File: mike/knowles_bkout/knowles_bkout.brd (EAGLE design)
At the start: 160 x 100 mm, 8 parts

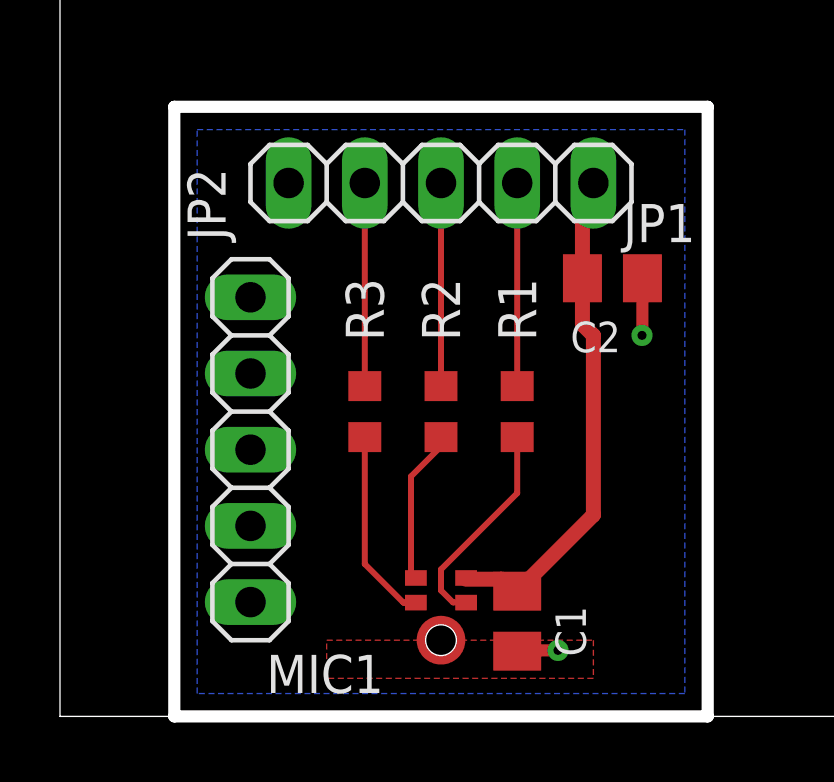
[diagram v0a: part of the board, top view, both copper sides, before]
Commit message: added leo footprint
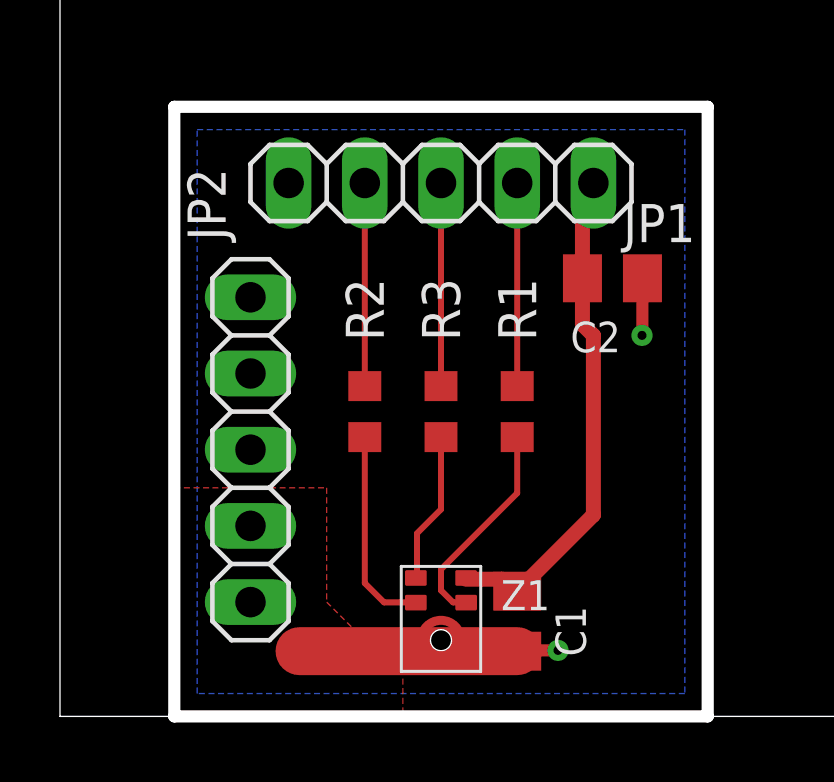
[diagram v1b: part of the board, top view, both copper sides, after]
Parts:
- removed MIC1: SPH0641LU4H-1, knowles_mic:SPH0641LU4H-1
- added Z1: SPH0641, SPH0641:SPH0641
- moved R2 2.54 mm to (10.2, 10.2)
- moved R3 2.54 mm to (12.7, 10.2)
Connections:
- net GND: now also Z1.3; no longer MIC1.3
- net N$2: now also R3.1; no longer R2.1
- net N$3: now also R2.1; no longer R3.1
- net N$5: now also Z1.1; no longer MIC1.2
- net N$6: now also Z1.2; no longer MIC1.1
- net N$7: now also Z1.4; no longer MIC1.4
- net VCC: now also Z1.5; no longer MIC1.5
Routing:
- net GND: track 3.28 -> 10.5 mm
- net N$6: track 5.18 -> 6.84 mm
- net N$5: track 6.47 -> 5.04 mm
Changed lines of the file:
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@@
 </autorouter>
 <elements>
-<element name="MIC1" library="knowles_mic" package="SPH0641LU4H-1" value="SPH0641LU4H-1" x="12.7" y="2.54" smashed="yes">
-<attribute name="NAME" x="6.88" y="0.78" size="1.27" layer="25"/>
-<attribute name="VALUE" x="8.18" y="6.84" size="1.27" layer="27"/>
-</element>
 <element name="C1" library="rcl" package="C0805K" value="100nF" x="15.24" y="3.175" smashed="yes" rot="R270">
 <attribute name="NAME" x="16.515" y="3.675" size="1.016" layer="25" rot="R270"/>
@@
 <attribute name="VALUE" x="13.335" y="10.795" size="1.27" layer="27" rot="R270"/>
 </element>
-<element name="R2" library="rcl" package="R0603" value="" x="12.7" y="10.16" smashed="yes" rot="R270">
+<element name="R2" library="rcl" package="R0603" value="" x="10.16" y="10.16" smashed="yes" rot="R270">
+<attribute name="NAME" x="9.525" y="14.605" size="1.27" layer="25" rot="R270"/>
+<attribute name="VALUE" x="8.255" y="10.795" size="1.27" layer="27" rot="R270"/>
+</element>
+<element name="R3" library="rcl" package="R0603" value="" x="12.7" y="10.16" smashed="yes" rot="R270">
 <attribute name="NAME" x="12.065" y="14.605" size="1.27" layer="25" rot="R270"/>
 <attribute name="VALUE" x="10.795" y="10.795" size="1.27" layer="27" rot="R270"/>
-</element>
-<element name="R3" library="rcl" package="R0603" value="" x="10.16" y="10.16" smashed="yes" rot="R270">
-<attribute name="NAME" x="9.525" y="14.605" size="1.27" layer="25" rot="R270"/>
-<attribute name="VALUE" x="8.255" y="10.795" size="1.27" layer="27" rot="R270"/>
 </element>
 <element name="JP2" library="pinhead" package="1X05" value="" x="6.35" y="8.89" smashed="yes" rot="R90">
@@
 <attribute name="VALUE" x="17.415" y="12.705" size="1.016" layer="27" display="off"/>
 </element>
+<element name="Z1" library="SPH0641" package="SPH0641" value="SPH0641" x="12.7" y="2.54"/>
 </elements>
 <signals>
 <signal name="GND">
 <contactref element="C1" pad="2"/>
-<contactref element="JP1" pad="1"/>
-<contactref element="JP2" pad="5"/>
-<contactref element="JP2" pad="4"/>
-<contactref element="JP2" pad="3"/>
-<contactref element="JP2" pad="2"/>
-<contactref element="JP2" pad="1"/>
 <contactref element="C2" pad="2"/>
 <polygon width="0.5" layer="16">
@@
 <wire x1="19.415" y1="12.715" x2="19.4" y2="12.7" width="0.4064" layer="1"/>
 <via x="19.4" y="12.7" extent="1-16" drill="0.3" diameter="0.6"/>
-<wire x1="15.24" y1="2.175" x2="15.265" y2="2.2" width="0.4064" layer="1"/>
 <wire x1="15.265" y1="2.2" x2="16.6" y2="2.2" width="0.4064" layer="1"/>
 <via x="16.6" y="2.2" extent="1-16" drill="0.3" diameter="0.6"/>
-<contactref element="MIC1" pad="3"/>
-<polygon width="0.2" layer="1" thermals="no">
-<vertex x="8.89" y="2.54"/>
-<vertex x="17.78" y="2.54"/>
-<vertex x="17.78" y="1.27"/>
-<vertex x="8.89" y="1.27"/>
+<contactref element="JP1" pad="1"/>
+<contactref element="JP2" pad="5"/>
+<contactref element="JP2" pad="4"/>
+<contactref element="JP2" pad="3"/>
+<contactref element="JP2" pad="2"/>
+<contactref element="JP2" pad="1"/>
+<contactref element="Z1" pad="3"/>
+<wire x1="15.24" y1="2.175" x2="7.985" y2="2.175" width="1.6" layer="1"/>
+<polygon width="0.45" layer="1">
+<vertex x="5.08" y="7.62"/>
+<vertex x="8.89" y="7.62"/>
+<vertex x="8.89" y="3.81"/>
+<vertex x="10.16" y="2.54"/>
+<vertex x="11.43" y="2.54"/>
+<vertex x="11.43" y="0"/>
+<vertex x="3.81" y="0"/>
+<vertex x="3.81" y="7.62"/>
 </polygon>
-<wire x1="15.24" y1="2.175" x2="12.7" y2="2.54" width="0" layer="19" extent="1-1"/>
+<wire x1="15.24" y1="2.175" x2="13.3625" y2="2.54" width="0" layer="19" extent="1-1"/>
 </signal>
 <signal name="VCC">
@@
 <wire x1="14.732" y1="4.175" x2="15.24" y2="4.175" width="0.5" layer="1"/>
 <wire x1="17.415" y1="17.415" x2="17.415" y2="14.605" width="0.5" layer="1"/>
-<contactref element="MIC1" pad="5"/>
 <contactref element="JP1" pad="5"/>
+<contactref element="Z1" pad="5"/>
 <wire x1="17.415" y1="17.415" x2="17.78" y2="17.78" width="0" layer="19" extent="1-1"/>
 <wire x1="13.5375" y1="4.614" x2="13.5375" y2="4.572" width="0" layer="19" extent="1-1"/>
@@
 <wire x1="15.24" y1="17.78" x2="15.24" y2="11.01" width="0.2" layer="1"/>
 </signal>
-<signal name="N$2">
-<contactref element="JP1" pad="3"/>
-<contactref element="R2" pad="1"/>
-<wire x1="12.7" y1="17.78" x2="12.7" y2="11.01" width="0.2" layer="1"/>
-</signal>
-<signal name="N$3">
-<contactref element="JP1" pad="2"/>
-<contactref element="R3" pad="1"/>
-<wire x1="10.16" y1="17.78" x2="10.16" y2="11.01" width="0.2" layer="1"/>
-</signal>
 <signal name="N$5">
-<contactref element="MIC1" pad="2"/>
 <contactref element="R3" pad="2"/>
-<wire x1="10.16" y1="9.31" x2="10.16" y2="5.08" width="0.2" layer="1"/>
-<wire x1="10.16" y1="5.08" x2="11.448" y2="3.792" width="0.2" layer="1"/>
-<wire x1="11.448" y1="3.792" x2="11.8625" y2="3.792" width="0.2" layer="1"/>
+<contactref element="Z1" pad="1"/>
+<wire x1="12.7" y1="9.31" x2="12.7" y2="6.9" width="0.2" layer="1"/>
+<wire x1="12.7" y1="6.9" x2="11.9" y2="6.1" width="0.2" layer="1"/>
+<wire x1="11.9" y1="6.1" x2="11.9" y2="4.6515" width="0.2" layer="1"/>
+<wire x1="11.9" y1="4.6515" x2="11.8625" y2="4.614" width="0.2" layer="1"/>
 </signal>
 <signal name="N$6">
-<contactref element="MIC1" pad="1"/>
 <contactref element="R2" pad="2"/>
-<wire x1="11.8625" y1="4.614" x2="11.7" y2="4.7765" width="0.2" layer="1"/>
-<wire x1="11.7" y1="4.7765" x2="11.7" y2="8" width="0.2" layer="1"/>
-<wire x1="11.7" y1="8" x2="12.7" y2="9" width="0.2" layer="1"/>
-<wire x1="12.7" y1="9" x2="12.7" y2="9.31" width="0.2" layer="1"/>
+<contactref element="Z1" pad="2"/>
+<wire x1="10.16" y1="9.31" x2="10.16" y2="4.44" width="0.2" layer="1"/>
+<wire x1="10.16" y1="4.44" x2="10.8" y2="3.8" width="0.2" layer="1"/>
+<wire x1="10.8" y1="3.8" x2="11.8545" y2="3.8" width="0.2" layer="1"/>
+<wire x1="11.8545" y1="3.8" x2="11.8625" y2="3.792" width="0.2" layer="1"/>
 </signal>
 <signal name="N$7">
-<contactref element="MIC1" pad="4"/>
 <contactref element="R1" pad="2"/>
-<wire x1="13.5375" y1="3.792" x2="13.5295" y2="3.8" width="0.2" layer="1"/>
 <wire x1="13.5295" y1="3.8" x2="13.1" y2="3.8" width="0.2" layer="1"/>
 <wire x1="13.1" y1="3.8" x2="12.7" y2="4.2" width="0.2" layer="1"/>
@@
 <wire x1="12.7" y1="4.9" x2="15.24" y2="7.44" width="0.2" layer="1"/>
 <wire x1="15.24" y1="7.44" x2="15.24" y2="9.31" width="0.2" layer="1"/>
+<contactref element="Z1" pad="4"/>
+<wire x1="13.5375" y1="3.792" x2="13.5295" y2="3.8" width="0" layer="19" extent="1-1"/>
+</signal>
+<signal name="N$2">
+<contactref element="JP1" pad="3"/>
+<contactref element="R3" pad="1"/>
+<wire x1="12.7" y1="11.01" x2="12.7" y2="17.78" width="0.2" layer="1"/>
+</signal>
+<signal name="N$3">
+<contactref element="JP1" pad="2"/>
+<contactref element="R2" pad="1"/>
+<wire x1="10.16" y1="11.01" x2="10.16" y2="17.78" width="0.2" layer="1"/>
 </signal>
 </signals>
